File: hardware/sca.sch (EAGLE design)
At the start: 34 parts

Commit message: added notes
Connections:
- new net XBEE_RST: U$9.27, XB1.!RESET
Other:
- note added: "1) Place Xbee decopling capacitors in order shown 2) Place capacitors as close to Xbee Vcc as possible"
- note added: "1) Place capacitors as close to regulator as possible"
- note added: "Main Control Unit"
- note added: "NOTES:"
- moved on the sheet: BNO055_H1, BNO055_H2, C1, C10, C11, C12, C13, C2, C3, U$9, XB1

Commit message: added 3.3 and 5 V dividers
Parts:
- removed JP4: (no value), microbuilder:HEADER-1X970MIL
- removed U$9: TEENSY_3.6_DIL, Teensy_3_and_LC_Series_Boards_v1.4:TEENSY_3.6_DIL
- added GPS_H: (no value), microbuilder:HEADER-1X970MIL
- added R11, R12, R13, R14: 1M, resistor:R-US_0309/10
- added TEENSY3.6: TEENSY_3.6_DIL, Teensy_3_and_LC_Series_Boards_v1.4:TEENSY_3.6_DIL
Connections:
- removed net MCU_2: R1.1, R2.1, U$9.2/PWM
- new net 3V3_V: R11.1, R12.1, TEENSY3.6.21/A7/PWM
- new net 5V_V: R13.1, R14.1, TEENSY3.6.22/A8/T/PWM
- new net BATT_V: R1.1, R2.1, TEENSY3.6.2/PWM
- net +3V3: now also R11.2, TEENSY3.6.VIN; no longer U$9.VIN
- net +5V: now also GPS_H.2, R13.2; no longer JP4.2
- net 1PPS: now also GPS_H.1; no longer JP4.1
- net ALT_SCL: now also TEENSY3.6.19/A5/T/SCL0; no longer U$9.19/A5/T/SCL0
- net ALT_SDA: now also TEENSY3.6.18/A4/T/SDA0; no longer U$9.18/A4/T/SDA0
- net BATT_T: now also TEENSY3.6.3/CAN0-TX/SCL2/PWM; no longer U$9.3/CAN0-TX/SCL2/PWM
- net FIX: now also GPS_H.6; no longer JP4.6
- net GND: now also GPS_H.3, R12.2, R14.2, TEENSY3.6.AGND, TEENSY3.6.GND; no longer JP4.3, U$9.AGND, U$9.GND
- net GPS_EN: now also GPS_H.8; no longer JP4.8
- net GPS_RX: now also GPS_H.4, TEENSY3.6.10/TX2/PWM; no longer JP4.4, U$9.10/TX2/PWM
- net GPS_TX: now also GPS_H.5, TEENSY3.6.9/RX2/PWM; no longer JP4.5, U$9.9/RX2/PWM
- net LED_1: now also TEENSY3.6.15/A1/T; no longer U$9.15/A1/T
- net LED_2: now also TEENSY3.6.13/SCK0/LED; no longer U$9.13/SCK0/LED
- net LED_3: now also TEENSY3.6.14/A0/PWM; no longer U$9.14/A0/PWM
- net N$3: now also GPS_H.9; no longer JP4.9
- net PR_1: now also TEENSY3.6.1/TX1/MISO1/T; no longer U$9.1/TX1/MISO1/T
- net PR_2: now also TEENSY3.6.4/CAN0-RX/SDA2/PWM; no longer U$9.4/CAN0-RX/SDA2/PWM
- net PR_3: now also TEENSY3.6.23/A9/T/PWM; no longer U$9.16/A2/T/PWM
- net PR_4: now also TEENSY3.6.0/RX1/MOSI1/T; no longer U$9.0/RX1/MOSI1/T
- net SCL: now also TEENSY3.6.37/A18/SCL1/PWM; no longer U$9.37/A18/SCL1/PWM
- net SDA: now also TEENSY3.6.38/A19/SDA1/PWM; no longer U$9.38/A19/SDA1/PWM
- net VBACKUP: now also GPS_H.7; no longer JP4.7
- net XBEE_EN: now also TEENSY3.6.28; no longer U$9.28
- net XBEE_RST: now also TEENSY3.6.27; no longer U$9.27
- net XBEE_RX: now also TEENSY3.6.32/A13/TX4; no longer U$9.32/A13/TX4
- net XBEE_TX: now also TEENSY3.6.31/A12/RX4; no longer U$9.31/A12/RX4
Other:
- note added: "Analog Sensors"
- note added: "Digital Sensors"
- note added: "Power"
- note removed: "DIGITAL SENSORS"
- note removed: "POWER"

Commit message: Updated PDF
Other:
- note added: "3V3 Reg"
- note added: "5V Reg"
- note added: "Altimeter"
- note added: "GPS"
- note added: "IMU"
- note added: "Indicator LEDs"
- note added: "Lipo Connector"
- note added: "MCU"
- note added: "Photoresistors"
- note added: "Thermistor"
- note added: "Voltage"
- note added: "Xbee"
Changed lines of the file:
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@@
 <text x="10.16" y="43.18" size="3.81" layer="97">NOTES:</text>
 <text x="99.06" y="162.56" size="6.35" layer="97">Main Control Unit</text>
+<text x="91.44" y="154.94" size="2.54" layer="97">MCU</text>
 </plain>
 <instances>
@@
 </instance>
 <instance part="+3V11" gate="G$1" x="173.99" y="147.32" smashed="yes" grouprefs="MCU">
-<attribute name="VALUE" x="171.45" y="142.24" size="1.778" layer="96" rot="R90"/>
+<attribute name="VALUE" x="171.45" y="147.32" size="1.778" layer="96" rot="R180"/>
 </instance>
 <instance part="U$11" gate="G$1" x="173.99" y="125.73" smashed="yes" grouprefs="MCU">
@@
 NASA Student Launch
 </text>
+<text x="45.72" y="121.92" size="2.54" layer="97">Lipo Connector</text>
+<text x="109.22" y="129.54" size="2.54" layer="97">5V Reg</text>
+<text x="180.34" y="124.46" size="2.54" layer="97">3V3 Reg</text>
 </plain>
 <instances>
@@
 </instance>
 <instance part="+3V2" gate="G$1" x="214.63" y="114.3" smashed="yes" grouprefs="3V3_REGULATOR">
-<attribute name="VALUE" x="212.09" y="109.22" size="1.778" layer="96" rot="R90"/>
+<attribute name="VALUE" x="219.71" y="116.84" size="1.778" layer="96" rot="R180"/>
 </instance>
 <instance part="P+3" gate="1" x="185.42" y="115.57" smashed="yes" grouprefs="3V3_REGULATOR">
-<attribute name="VALUE" x="182.88" y="110.49" size="1.778" layer="96" rot="R90"/>
+<attribute name="VALUE" x="190.5" y="118.11" size="1.778" layer="96" rot="R180"/>
 </instance>
 <instance part="5V_REG" gate="A1" x="128.27" y="105.41" smashed="yes" grouprefs="5V_REGULATOR">
@@
 </instance>
 <instance part="SUPPLY2" gate="G$1" x="114.3" y="116.84" smashed="yes" grouprefs="5V_REGULATOR">
-<attribute name="VALUE" x="114.3" y="119.634" size="1.778" layer="96" align="bottom-center"/>
+<attribute name="VALUE" x="119.38" y="119.634" size="1.778" layer="96" align="bottom-center"/>
 </instance>
 <instance part="U$3" gate="G$1" x="128.27" y="90.17" smashed="yes" grouprefs="5V_REGULATOR"/>
@@
 </instance>
 <instance part="P+2" gate="1" x="143.51" y="111.76" smashed="yes" grouprefs="5V_REGULATOR">
-<attribute name="VALUE" x="138.43" y="109.22" size="1.778" layer="96" rot="R90"/>
+<attribute name="VALUE" x="146.05" y="111.76" size="1.778" layer="96"/>
 </instance>
 <instance part="U$5" gate="G$1" x="58.42" y="101.6" smashed="yes" rot="R180" grouprefs="BATT_CONNECTOR"/>
@@
 NASA Student Launch
 </text>
+<text x="30.48" y="154.94" size="2.54" layer="97">Xbee</text>
+<text x="142.24" y="152.4" size="2.54" layer="97">IMU</text>
+<text x="127" y="109.22" size="2.54" layer="97">GPS</text>
+<text x="198.12" y="109.22" size="2.54" layer="97">Altimeter</text>
 </plain>
 <instances>
@@
 </instance>
 <instance part="P+9" gate="1" x="176.53" y="142.24" smashed="yes" grouprefs="BNO055_IMU">
-<attribute name="VALUE" x="176.53" y="144.78" size="1.778" layer="96" rot="R180"/>
+<attribute name="VALUE" x="181.61" y="144.78" size="1.778" layer="96" rot="R180"/>
 </instance>
 <instance part="U$6" gate="G$1" x="231.14" y="83.82" smashed="yes" grouprefs="BMP338">
@@
 </instance>
 <instance part="+3V4" gate="G$1" x="92.71" y="91.44" smashed="yes" grouprefs="XBEE">
-<attribute name="VALUE" x="95.25" y="93.98" size="1.778" layer="96" rot="R180"/>
+<attribute name="VALUE" x="97.79" y="93.98" size="1.778" layer="96" rot="R180"/>
 </instance>
 <instance part="C1" gate="G$1" x="68.58" y="85.09" smashed="yes" grouprefs="XBEE">
@@
 NASA Student Launch
 </text>
+<text x="25.4" y="152.4" size="2.54" layer="97">Photoresistors</text>
+<text x="50.8" y="104.14" size="2.54" layer="97">Thermistor</text>
+<text x="134.62" y="104.14" size="2.54" layer="97">Voltage</text>
+<text x="152.4" y="147.32" size="2.54" layer="97">Indicator LEDs</text>
 </plain>
 <instances>
@@
 </instance>
 <instance part="U$13" gate="G$1" x="171.45" y="63.5" smashed="yes" grouprefs="VOLTAGE">
-<attribute name="VALUE" x="177.546" y="64.77" size="1.27" layer="96" rot="R180"/>
+<attribute name="VALUE" x="169.926" y="64.77" size="1.27" layer="96" rot="R180"/>
 </instance>
 <instance part="+3V1" gate="G$1" x="139.7" y="71.12" smashed="yes" rot="MR0" grouprefs="VOLTAGE">
@@
 </instance>
 <instance part="U$14" gate="G$1" x="212.09" y="73.66" smashed="yes" grouprefs="VOLTAGE">
-<attribute name="VALUE" x="218.186" y="74.93" size="1.27" layer="96" rot="R180"/>
+<attribute name="VALUE" x="210.566" y="74.93" size="1.27" layer="96" rot="R180"/>
 </instance>
 <instance part="+5V" gate="1" x="181.61" y="81.28" smashed="yes" grouprefs="VOLTAGE">

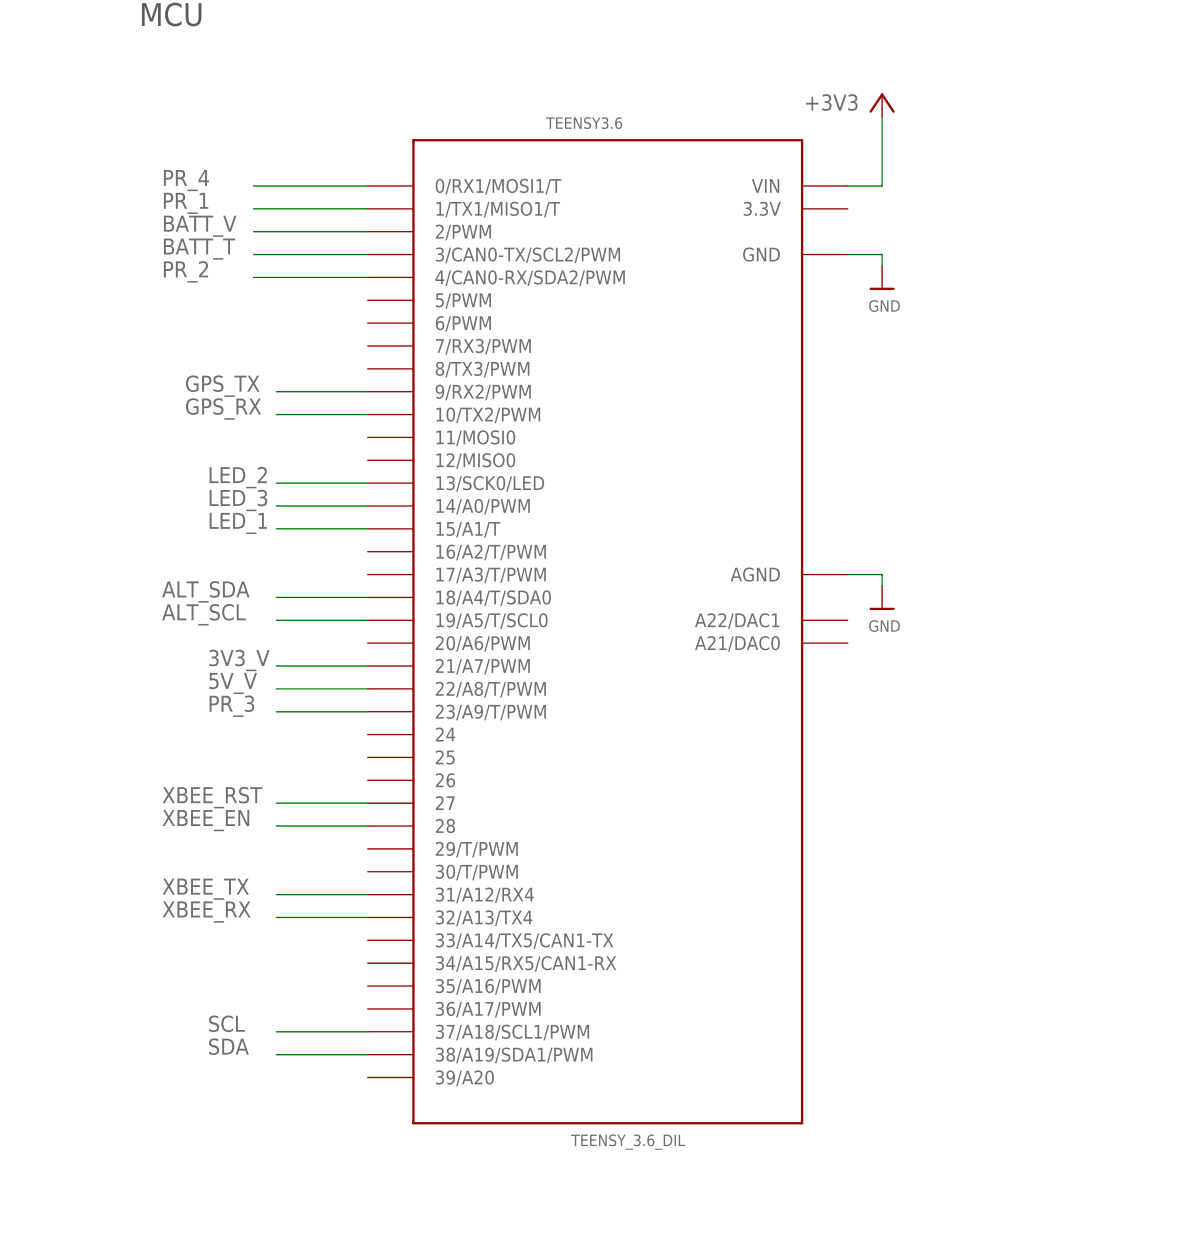
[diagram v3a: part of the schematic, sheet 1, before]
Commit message: corrected analog output pins
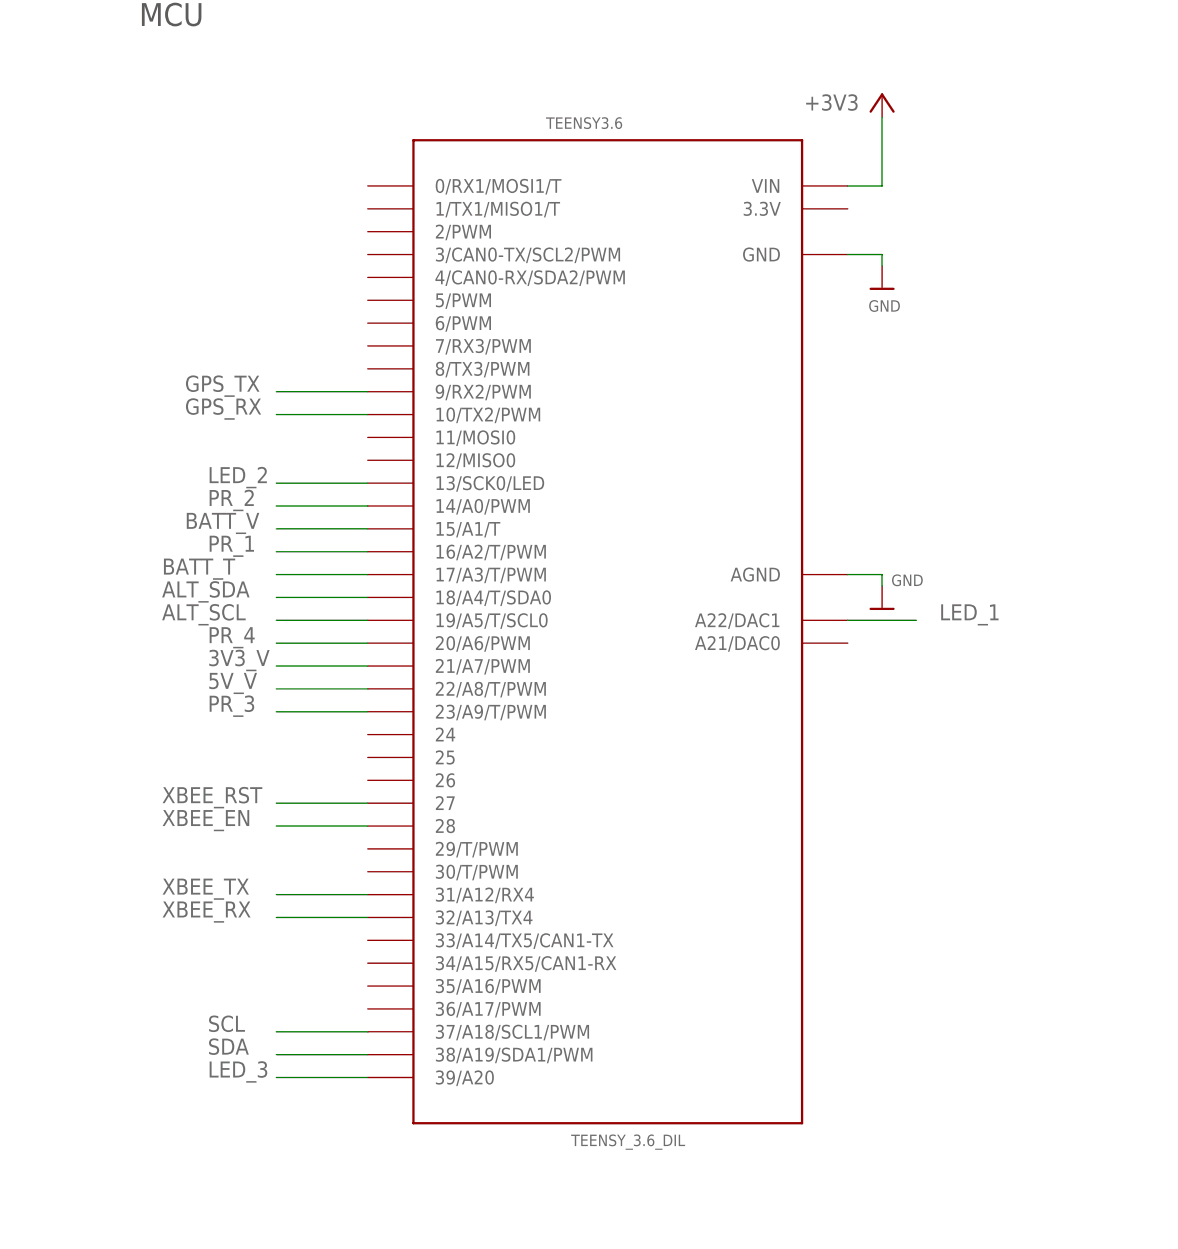
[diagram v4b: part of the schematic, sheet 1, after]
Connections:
- net BATT_T: now also TEENSY3.6.17/A3/T/PWM; no longer TEENSY3.6.3/CAN0-TX/SCL2/PWM
- net BATT_V: now also TEENSY3.6.15/A1/T; no longer TEENSY3.6.2/PWM
- net LED_1: now also TEENSY3.6.A22/DAC1; no longer TEENSY3.6.15/A1/T
- net LED_3: now also TEENSY3.6.39/A20; no longer TEENSY3.6.14/A0/PWM
- net PR_1: now also TEENSY3.6.16/A2/T/PWM; no longer TEENSY3.6.1/TX1/MISO1/T
- net PR_2: now also TEENSY3.6.14/A0/PWM; no longer TEENSY3.6.4/CAN0-RX/SDA2/PWM
- net PR_4: now also TEENSY3.6.20/A6/PWM; no longer TEENSY3.6.0/RX1/MOSI1/T
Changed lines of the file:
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@@
 </instance>
 <instance part="U$1" gate="G$1" x="173.99" y="90.17" smashed="yes" grouprefs="MCU">
-<attribute name="VALUE" x="172.466" y="87.63" size="1.27" layer="96"/>
+<attribute name="VALUE" x="175.006" y="92.71" size="1.27" layer="96"/>
 </instance>
 <instance part="FRAME2" gate="G$1" x="0" y="0" smashed="yes">
@@
 </segment>
 </net>
-<net name="BATT_V" class="0">
-<segment>
-<pinref part="TEENSY3.6" gate="G$1" pin="2/PWM"/>
-<wire x1="116.84" y1="132.08" x2="104.14" y2="132.08" width="0.1524" layer="91" grouprefs="MCU"/>
-<label x="93.98" y="132.08" size="1.778" layer="95" grouprefs="MCU"/>
-</segment>
-</net>
 <net name="GPS_TX" class="0">
 <segment>
@@
 <net name="LED_1" class="0">
 <segment>
-<pinref part="TEENSY3.6" gate="G$1" pin="15/A1/T"/>
-<wire x1="116.84" y1="99.06" x2="106.68" y2="99.06" width="0.1524" layer="91" grouprefs="MCU"/>
-<label x="99.06" y="99.06" size="1.778" layer="95" grouprefs="MCU"/>
+<pinref part="TEENSY3.6" gate="G$1" pin="A22/DAC1"/>
+<wire x1="170.18" y1="88.9" x2="177.8" y2="88.9" width="0.1524" layer="91"/>
+<label x="180.34" y="88.9" size="1.778" layer="95" grouprefs="MCU"/>
 </segment>
 </net>
 <net name="LED_3" class="0">
 <segment>
-<pinref part="TEENSY3.6" gate="G$1" pin="14/A0/PWM"/>
-<wire x1="116.84" y1="101.6" x2="106.68" y2="101.6" width="0.1524" layer="91" grouprefs="MCU"/>
-<label x="99.06" y="101.6" size="1.778" layer="95" grouprefs="MCU"/>
-</segment>
-</net>
-<net name="PR_1" class="0">
-<segment>
-<pinref part="TEENSY3.6" gate="G$1" pin="1/TX1/MISO1/T"/>
-<wire x1="116.84" y1="134.62" x2="104.14" y2="134.62" width="0.1524" layer="91" grouprefs="MCU"/>
-<label x="93.98" y="134.62" size="1.778" layer="95" grouprefs="MCU"/>
+<pinref part="TEENSY3.6" gate="G$1" pin="39/A20"/>
+<wire x1="116.84" y1="38.1" x2="106.68" y2="38.1" width="0.1524" layer="91"/>
+<label x="99.06" y="38.1" size="1.778" layer="95"/>
 </segment>
 </net>
 <net name="PR_2" class="0">
 <segment>
-<pinref part="TEENSY3.6" gate="G$1" pin="4/CAN0-RX/SDA2/PWM"/>
-<wire x1="116.84" y1="127" x2="104.14" y2="127" width="0.1524" layer="91" grouprefs="MCU"/>
-<label x="93.98" y="127" size="1.778" layer="95" grouprefs="MCU"/>
+<pinref part="TEENSY3.6" gate="G$1" pin="14/A0/PWM"/>
+<wire x1="116.84" y1="101.6" x2="106.68" y2="101.6" width="0.1524" layer="91"/>
+<label x="99.06" y="101.6" size="1.778" layer="95"/>
 </segment>
 </net>
@@
 <wire x1="116.84" y1="78.74" x2="106.68" y2="78.74" width="0.1524" layer="91"/>
 <label x="99.06" y="78.74" size="1.778" layer="95"/>
-</segment>
-</net>
-<net name="PR_4" class="0">
-<segment>
-<pinref part="TEENSY3.6" gate="G$1" pin="0/RX1/MOSI1/T"/>
-<wire x1="116.84" y1="137.16" x2="104.14" y2="137.16" width="0.1524" layer="91" grouprefs="MCU"/>
-<label x="93.98" y="137.16" size="1.778" layer="95" grouprefs="MCU"/>
 </segment>
 </net>
@@
 <wire x1="173.99" y1="92.71" x2="173.99" y2="93.98" width="0.1524" layer="91" grouprefs="MCU"/>
 <wire x1="173.99" y1="93.98" x2="170.18" y2="93.98" width="0.1524" layer="91" grouprefs="MCU"/>
-</segment>
-</net>
-<net name="BATT_T" class="0">
-<segment>
-<pinref part="TEENSY3.6" gate="G$1" pin="3/CAN0-TX/SCL2/PWM"/>
-<wire x1="116.84" y1="129.54" x2="104.14" y2="129.54" width="0.1524" layer="91" grouprefs="MCU"/>
-<label x="93.98" y="129.54" size="1.778" layer="95" grouprefs="MCU"/>
 </segment>
 </net>
@@
 </segment>
 </net>
+<net name="PR_4" class="0">
+<segment>
+<pinref part="TEENSY3.6" gate="G$1" pin="20/A6/PWM"/>
+<wire x1="116.84" y1="86.36" x2="106.68" y2="86.36" width="0.1524" layer="91"/>
+<label x="99.06" y="86.36" size="1.778" layer="95"/>
+</segment>
+</net>
+<net name="BATT_V" class="0">
+<segment>
+<pinref part="TEENSY3.6" gate="G$1" pin="15/A1/T"/>
+<wire x1="116.84" y1="99.06" x2="106.68" y2="99.06" width="0.1524" layer="91"/>
+<label x="96.52" y="99.06" size="1.778" layer="95"/>
+</segment>
+</net>
+<net name="PR_1" class="0">
+<segment>
+<pinref part="TEENSY3.6" gate="G$1" pin="16/A2/T/PWM"/>
+<wire x1="116.84" y1="96.52" x2="106.68" y2="96.52" width="0.1524" layer="91"/>
+<label x="99.06" y="96.52" size="1.778" layer="95"/>
+</segment>
+</net>
+<net name="BATT_T" class="0">
+<segment>
+<pinref part="TEENSY3.6" gate="G$1" pin="17/A3/T/PWM"/>
+<wire x1="116.84" y1="93.98" x2="106.68" y2="93.98" width="0.1524" layer="91"/>
+<label x="93.98" y="93.98" size="1.778" layer="95"/>
+</segment>
+</net>
